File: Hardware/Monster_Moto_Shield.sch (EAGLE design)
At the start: 44 parts, among them Q1 FDD8580, Q2 FDD8580, U1 VNH2SP30, U2 VNH2SP30, U3 ARDUINO_SHIELDLABEL

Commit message: Commit bec of computer change
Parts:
- removed U$6: CREATIVE_COMMONS, SparkFun:CREATIVE_COMMONS
- added FRAME*: FRAME-LETTER, SparkFun-Aesthetics:FRAME-LETTER
- U3: value ARDUINO_SHIELDLABEL -> ARDUINO_R3_SHIELD; device SparkFun:ARDUINO_SHIELDLABEL -> SparkFun-Boards:ARDUINO_R3_SHIELD
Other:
- note added: "J. Lindblom and N. Bernstein"
- note added: "Revised by: Patrick Alberts"
- note added: "V10"
- note removed: "Jim Lindblom"
- note removed: "Nate Bernstein"
- moved on the sheet: JP1, JP2, JP3, LED1, LED2, LED3, LED4, LED5, R18, R19, R20

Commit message: Cleared Up Drc Isssues
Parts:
- C1, C4: device SparkFun:CAP0402-CAP -> SparkFun-Capacitors:CAP0603-CAP
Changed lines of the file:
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@@
 <?xml version="1.0" encoding="utf-8"?>
 <!DOCTYPE eagle SYSTEM "eagle.dtd">
-<eagle version="6.4">
+<eagle version="6.5.0">
 <drawing>
 <settings>
@@
 <part name="R5" library="SparkFun-Resistors" deviceset="10KOHM1/10W1%(0603)" device="0603" value="10K"/>
 <part name="R6" library="SparkFun-Resistors" deviceset="1.5KOHM1/10W1%(0603)" device="" value="1.5K"/>
-<part name="C1" library="SparkFun" deviceset="CAP" device="0402-CAP" value="33nF"/>
+<part name="C1" library="SparkFun-Capacitors" deviceset="CAP" device="0603-CAP" value="33nF"/>
 <part name="GND6" library="SparkFun" deviceset="GND" device=""/>
 <part name="GND7" library="SparkFun" deviceset="GND" device=""/>
@@
 <part name="R14" library="SparkFun-Resistors" deviceset="10KOHM1/10W1%(0603)" device="0603" value="10K"/>
 <part name="R15" library="SparkFun-Resistors" deviceset="1.5KOHM1/10W1%(0603)" device="" value="1.5K"/>
-<part name="C4" library="SparkFun" deviceset="CAP" device="0402-CAP" value="33nF"/>
+<part name="C4" library="SparkFun-Capacitors" deviceset="CAP" device="0603-CAP" value="33nF"/>
 <part name="GND2" library="SparkFun" deviceset="GND" device=""/>
 <part name="GND4" library="SparkFun" deviceset="GND" device=""/>

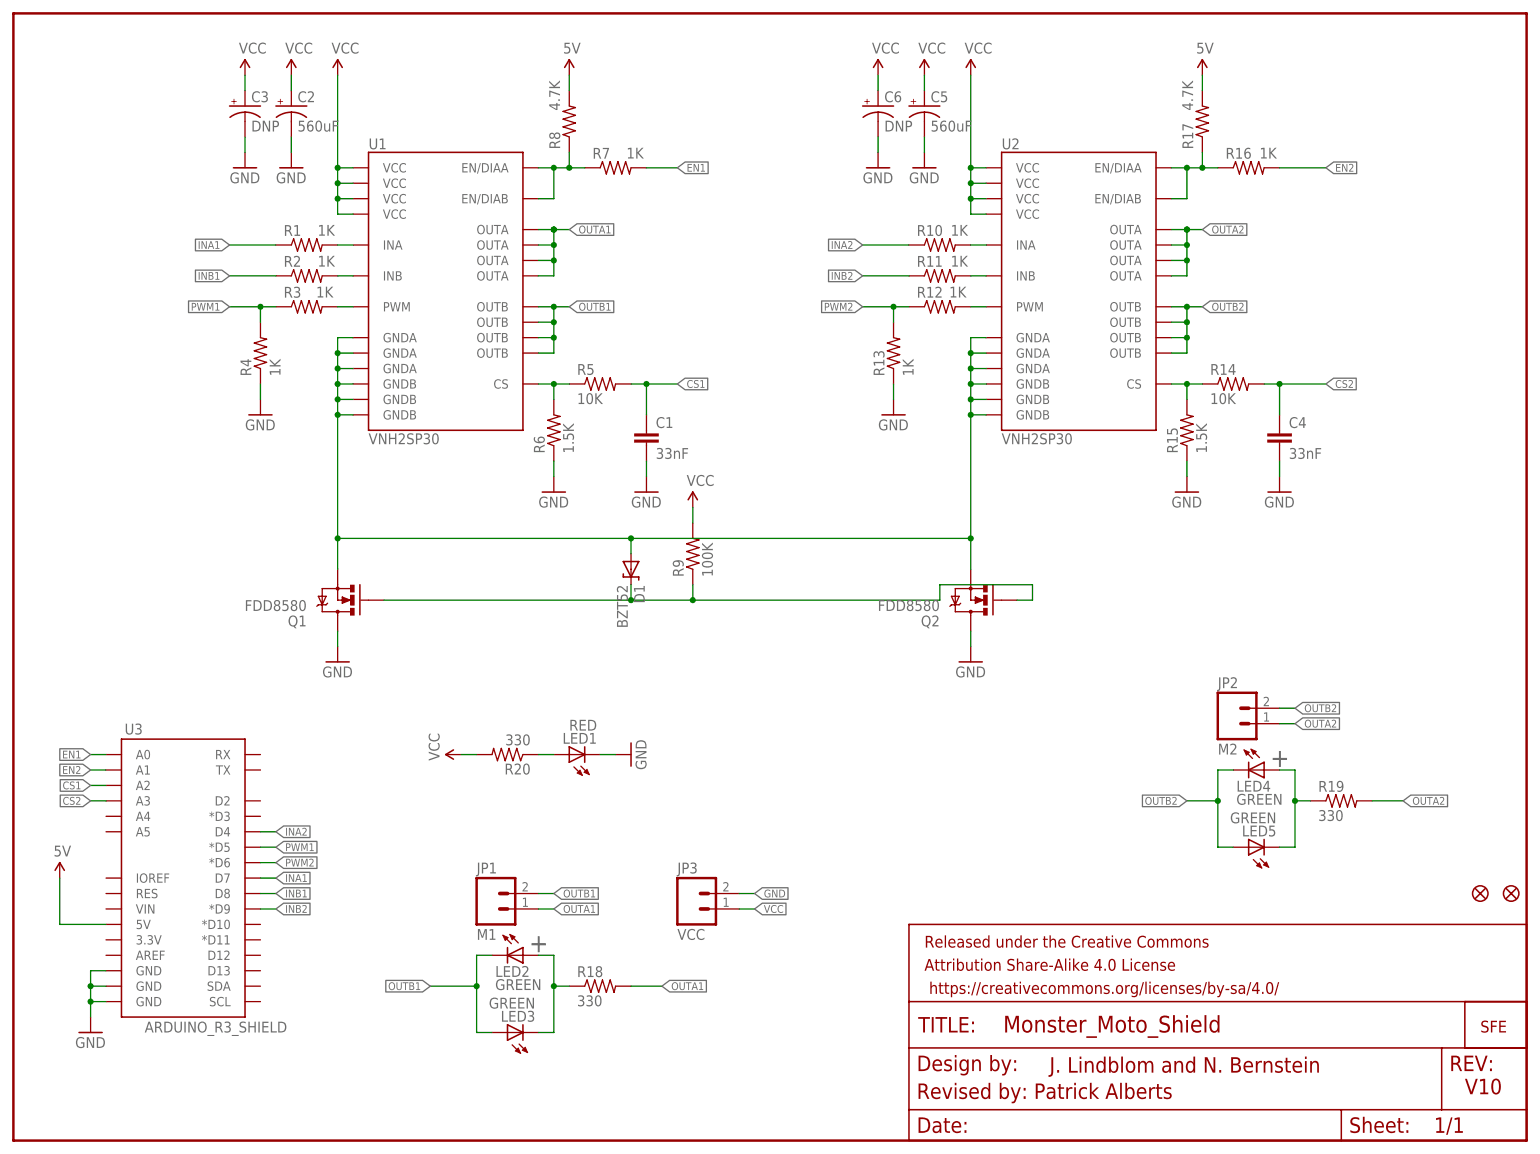
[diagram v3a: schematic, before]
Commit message: Added SF Flame, Cleaned Up SCH, Added Input v silk.
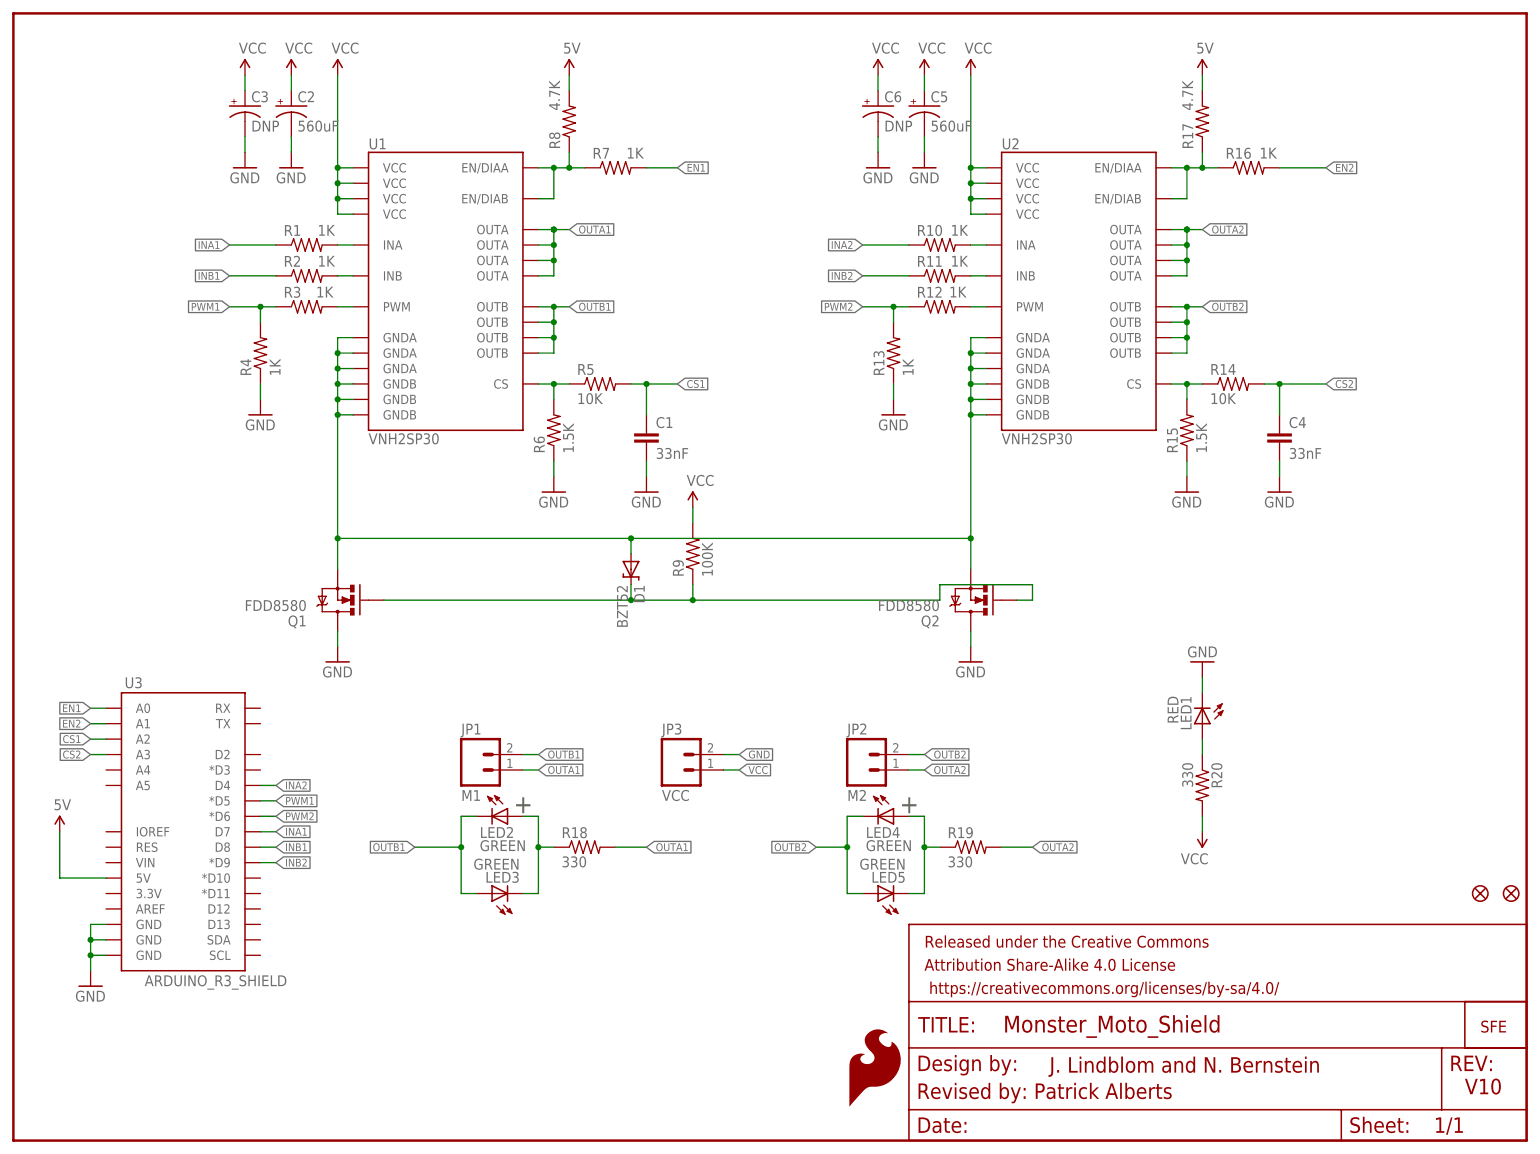
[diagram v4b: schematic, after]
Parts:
- added LOGO1: SFE_LOGO_FLAME.2_INCH, SparkFun-Aesthetics:SFE_LOGO_FLAME.2_INCH
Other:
- moved on the sheet: JP1, JP2, JP3, LED1, LED2, LED3, LED4, LED5, R18, R19, R20, U3

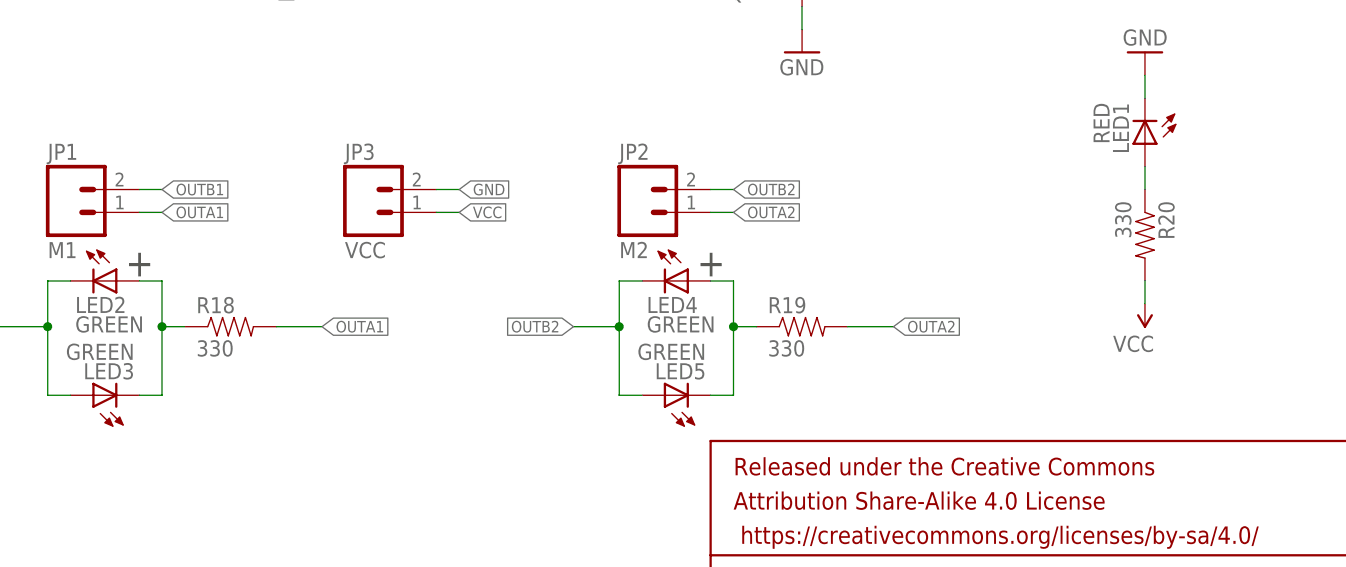
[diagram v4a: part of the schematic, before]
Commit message: Chaned LED res to 1k
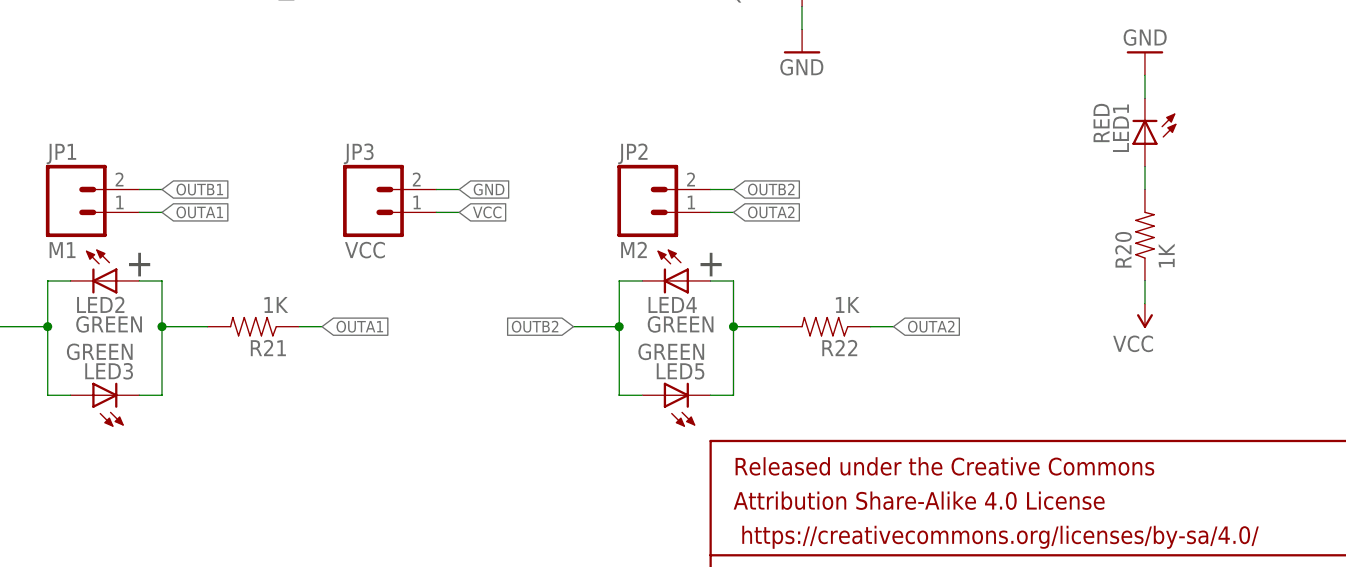
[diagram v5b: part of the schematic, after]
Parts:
- removed R18, R19: 330, SparkFun-Resistors:33OHM1/10W1%(0603)
- added R21, R22: 1K, SparkFun-Resistors:1KOHM1/10W1%(0603)
- R20: value 330 -> 1K; device SparkFun-Resistors:33OHM1/10W1%(0603) -> SparkFun-Resistors:1KOHM1/10W1%(0603)
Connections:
- net N$14: now also R21.2; no longer R18.1
- net N$16: now also R22.2; no longer R19.1
- net N$18: now also R20.2; no longer R20.1
- net OUTA1: now also R21.1; no longer R18.2
- net OUTA2: now also R22.1; no longer R19.2
- net VCC: now also R20.1; no longer R20.2
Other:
- moved on the sheet: R20
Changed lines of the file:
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@@
 <?xml version="1.0" encoding="utf-8"?>
 <!DOCTYPE eagle SYSTEM "eagle.dtd">
-<eagle version="6.5.0">
+<eagle version="6.4">
 <drawing>
 <settings>
@@
 <part name="LED4" library="SparkFun-LED" deviceset="LED-GREEN" device="0603" value="GREEN"/>
 <part name="LED5" library="SparkFun-LED" deviceset="LED-GREEN" device="0603" value="GREEN"/>
-<part name="R18" library="SparkFun-Resistors" deviceset="33OHM1/10W1%(0603)" device="" value="330"/>
-<part name="R19" library="SparkFun-Resistors" deviceset="33OHM1/10W1%(0603)" device="" value="330"/>
-<part name="R20" library="SparkFun-Resistors" deviceset="33OHM1/10W1%(0603)" device="" value="330"/>
 <part name="P+5" library="SparkFun" deviceset="VCC" device=""/>
 <part name="JP5" library="SparkFun" deviceset="LOGO-SFE" device="NEW"/>
@@
 <part name="JP6" library="SparkFun" deviceset="FIDUCIAL" device="1X2"/>
 <part name="LOGO1" library="SparkFun-Aesthetics" deviceset="SFE_LOGO_FLAME" device=".2_INCH"/>
+<part name="R20" library="SparkFun-Resistors" deviceset="1KOHM1/10W1%(0603)" device="" value="1K"/>
+<part name="R21" library="SparkFun-Resistors" deviceset="1KOHM1/10W1%(0603)" device="" value="1K"/>
+<part name="R22" library="SparkFun-Resistors" deviceset="1KOHM1/10W1%(0603)" device="" value="1K"/>
 </parts>
 <sheets>
@@
 <instance part="LED4" gate="G$1" x="144.78" y="53.34" rot="R270"/>
 <instance part="LED5" gate="G$1" x="142.24" y="40.64" rot="R90"/>
-<instance part="R18" gate="G$1" x="93.98" y="48.26" smashed="yes">
-<attribute name="NAME" x="90.17" y="49.7586" size="1.778" layer="95"/>
-<attribute name="VALUE" x="90.17" y="44.958" size="1.778" layer="96"/>
-</instance>
-<instance part="R19" gate="G$1" x="157.48" y="48.26"/>
-<instance part="R20" gate="G$1" x="195.58" y="58.42" rot="R270"/>
 <instance part="P+5" gate="1" x="195.58" y="50.8" rot="R180"/>
 <instance part="JP5" gate="G$1" x="241.3" y="17.78"/>
@@
 <instance part="JP6" gate="G$1" x="241.3" y="40.64"/>
 <instance part="LOGO1" gate="G$1" x="137.16" y="5.08"/>
+<instance part="R20" gate="G$1" x="195.58" y="58.42" rot="R90"/>
+<instance part="R21" gate="G$1" x="96.52" y="48.26" rot="R180"/>
+<instance part="R22" gate="G$1" x="160.02" y="48.26" rot="R180"/>
 </instances>
 <busses>
@@
 </segment>
 <segment>
-<wire x1="104.14" y1="48.26" x2="99.06" y2="48.26" width="0.1524" layer="91"/>
-<pinref part="R18" gate="G$1" pin="2"/>
+<wire x1="104.14" y1="48.26" x2="101.6" y2="48.26" width="0.1524" layer="91"/>
 <label x="104.14" y="48.26" size="1.27" layer="95" xref="yes"/>
+<pinref part="R21" gate="G$1" pin="1"/>
 </segment>
 </net>
@@
 <segment>
 <wire x1="195.58" y1="50.8" x2="195.58" y2="53.34" width="0.1524" layer="91"/>
-<pinref part="R20" gate="G$1" pin="2"/>
 <pinref part="P+5" gate="1" pin="VCC"/>
+<pinref part="R20" gate="G$1" pin="1"/>
 </segment>
 </net>
@@
 </segment>
 <segment>
-<wire x1="162.56" y1="48.26" x2="167.64" y2="48.26" width="0.1524" layer="91"/>
-<pinref part="R19" gate="G$1" pin="2"/>
+<wire x1="165.1" y1="48.26" x2="167.64" y2="48.26" width="0.1524" layer="91"/>
 <label x="167.64" y="48.26" size="1.27" layer="95" xref="yes"/>
+<pinref part="R22" gate="G$1" pin="1"/>
 </segment>
 </net>
@@
 <wire x1="149.86" y1="53.34" x2="149.86" y2="48.26" width="0.1524" layer="91"/>
 <wire x1="149.86" y1="48.26" x2="149.86" y2="40.64" width="0.1524" layer="91"/>
-<wire x1="149.86" y1="48.26" x2="152.4" y2="48.26" width="0.1524" layer="91"/>
+<wire x1="149.86" y1="48.26" x2="154.94" y2="48.26" width="0.1524" layer="91"/>
 <junction x="149.86" y="48.26"/>
 <pinref part="LED4" gate="G$1" pin="A"/>
 <pinref part="LED5" gate="G$1" pin="C"/>
-<pinref part="R19" gate="G$1" pin="1"/>
+<pinref part="R22" gate="G$1" pin="2"/>
 </segment>
 </net>
@@
 <wire x1="195.58" y1="66.04" x2="195.58" y2="63.5" width="0.1524" layer="91"/>
 <pinref part="LED1" gate="G$1" pin="A"/>
-<pinref part="R20" gate="G$1" pin="1"/>
+<pinref part="R20" gate="G$1" pin="2"/>
 </segment>
 </net>
@@
 <wire x1="86.36" y1="53.34" x2="86.36" y2="48.26" width="0.1524" layer="91"/>
 <wire x1="86.36" y1="48.26" x2="86.36" y2="40.64" width="0.1524" layer="91"/>
-<wire x1="86.36" y1="48.26" x2="88.9" y2="48.26" width="0.1524" layer="91"/>
+<wire x1="86.36" y1="48.26" x2="91.44" y2="48.26" width="0.1524" layer="91"/>
 <junction x="86.36" y="48.26"/>
 <pinref part="LED2" gate="G$1" pin="A"/>
 <pinref part="LED3" gate="G$1" pin="C"/>
-<pinref part="R18" gate="G$1" pin="1"/>
-</segment>
-</net>
+<pinref part="R21" gate="G$1" pin="2"/>
+</segment>
+</net>
